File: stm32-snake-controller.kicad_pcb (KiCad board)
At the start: 4 copper layers, 98 x 72 mm, 72 parts, among them J101 Barrel_Jack_MountingPin, J102 JST 2.54 Header, J103 Tag Connector, J301 Conn_01x03, J302 Conn_01x03, J401 Conn_01x07, J402 Conn_01x07, J501 USB_A, Q101 AO3501A, SW101 SW_Push, U101 USBLC6-2SC6, U102 M24C64-RMN, U103 STM32F401RCTx, U201 XC6220B331MR-G, U301 74AHCT1G125, U302 74AHCT1G125, U501 STMPS2141STR, Y101 32.768kHz, Y102 16MHz

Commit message: update BOM
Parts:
- U103: value STM32F401RCTx -> STM32F446RCTx
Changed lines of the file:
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@@
     (fp_line (start 1 0.6) (end -1 0.6)
       (stroke (width 0.1) (type solid)) (layer "F.Fab"))
-    (pad "1" smd roundrect (at -1.025 0 180) (size 1.15 1.4) (layers "F.Cu" "F.Paste" "F.Mask") (roundrect_rratio 0.217391)
+    (pad "1" smd roundrect (at -1.025 0 180) (size 1.15 1.4) (layers "F.Cu" "F.Paste" "F.Mask") (roundrect_rratio 0.2173913043)
       (net 9 "+3.3VA") (pintype "passive"))
-    (pad "2" smd roundrect (at 1.025 0 180) (size 1.15 1.4) (layers "F.Cu" "F.Paste" "F.Mask") (roundrect_rratio 0.217391)
+    (pad "2" smd roundrect (at 1.025 0 180) (size 1.15 1.4) (layers "F.Cu" "F.Paste" "F.Mask") (roundrect_rratio 0.2173913043)
       (net 8 "+3V3") (pintype "passive"))
     (model "${KICAD6_3DMODEL_DIR}/Inductor_SMD.3dshapes/L_0805_2012Metric.wrl"
@@
     (fp_line (start 7.95 2.8) (end 7.95 -1.7)
       (stroke (width 0.1) (type solid)) (layer "F.Fab"))
-    (pad "1" thru_hole roundrect (at 0 0 180) (size 1.2 1.75) (drill 0.75) (layers "*.Cu" "*.Mask") (roundrect_rratio 0.208333)
+    (pad "1" thru_hole roundrect (at 0 0 180) (size 1.2 1.75) (drill 0.75) (layers "*.Cu" "*.Mask") (roundrect_rratio 0.2083333333)
       (net 13 "+5V") (pinfunction "Pin_1") (pintype "passive"))
     (pad "2" thru_hole oval (at 2 0 180) (size 1.2 1.75) (drill 0.75) (layers "*.Cu" "*.Mask")
@@
     (descr "Mounting Hole 3.2mm, no annular, M3")
     (tags "mounting hole 3.2mm no annular m3")
+    (property "LCSC" "")
+    (property "Mouser" "")
     (property "Sheetfile" "stm32-snake-controller.kicad_sch")
     (property "Sheetname" "")
+    (property "exclude_from_bom" "")
     (property "ki_description" "Mounting Hole without connection")
     (property "ki_keywords" "mounting hole")
-    (attr exclude_from_pos_files)
+    (attr exclude_from_pos_files exclude_from_bom)
     (fp_text reference "H102" (at 0 -4.2) (layer "F.SilkS") hide
         (effects (font (size 1 1) (thickness 0.15)))
@@
     (property "Sheetfile" "stm32-snake-controller.kicad_sch")
     (property "Sheetname" "")
+    (property "exclude_from_bom" "")
     (property "ki_description" "DC Barrel Jack with a mounting pin")
     (property "ki_keywords" "DC power barrel jack connector")
-    (attr through_hole)
+    (attr through_hole exclude_from_bom)
     (fp_text reference "J101" (at 0 2.794 180 unlocked) (layer "F.SilkS") hide
         (effects (font (size 1 1) (thickness 0.15)))
@@
     (descr "Mounting Hole 3.2mm, no annular, M3")
     (tags "mounting hole 3.2mm no annular m3")
+    (property "LCSC" "")
+    (property "Mouser" "")
     (property "Sheetfile" "stm32-snake-controller.kicad_sch")
     (property "Sheetname" "")
+    (property "exclude_from_bom" "")
     (property "ki_description" "Mounting Hole without connection")
     (property "ki_keywords" "mounting hole")
-    (attr exclude_from_pos_files)
+    (attr exclude_from_pos_files exclude_from_bom)
     (fp_text reference "H101" (at 0 -4.2) (layer "F.SilkS") hide
         (effects (font (size 1 1) (thickness 0.15)))
@@
   (footprint "User_Footprint:SNES_Controller_Port_Horizontal" (layer "F.Cu")
     (at 175.5 121.805)
+    (property "LCSC" "")
+    (property "Mouser" "")
     (property "Sheetfile" "snes_controller.kicad_sch")
     (property "Sheetname" "snes_controller")
+    (property "exclude_from_bom" "")
     (property "ki_description" "Generic connector, single row, 01x07, script generated (kicad-library-utils/schlib/autogen/connector/)")
     (property "ki_keywords" "connector")
-    (attr through_hole)
+    (attr through_hole exclude_from_bom)
     (fp_text reference "J401" (at -0.018 -3.6 unlocked) (layer "F.SilkS") hide
         (effects (font (size 1 1) (thickness 0.12)))
@@
     (fp_line (start 7.95 2.8) (end 7.95 -1.7)
       (stroke (width 0.1) (type solid)) (layer "F.Fab"))
-    (pad "1" thru_hole roundrect (at 0 0 90) (size 1.2 1.75) (drill 0.75) (layers "*.Cu" "*.Mask") (roundrect_rratio 0.208333)
+    (pad "1" thru_hole roundrect (at 0 0 90) (size 1.2 1.75) (drill 0.75) (layers "*.Cu" "*.Mask") (roundrect_rratio 0.2083333333)
       (net 2 "GND") (pinfunction "GND") (pintype "power_in"))
     (pad "2" thru_hole oval (at 2 0 90) (size 1.2 1.75) (drill 0.75) (layers "*.Cu" "*.Mask")
@@
     (descr "LQFP, 64 Pin (https://www.analog.com/media/en/technical-documentation/data-sheets/ad7606_7606-6_7606-4.pdf), generated with kicad-footprint-generator ipc_gullwing_generator.py")
     (tags "LQFP QFP")
-    (property "LCSC" "C74524")
+    (property "LCSC" "C915971")
     (property "Sheetfile" "stm32-snake-controller.kicad_sch")
     (property "Sheetname" "")
@@
         (effects (font (size 1 1) (thickness 0.15)))
     )
-    (fp_text value "STM32F401RCTx" (at 0 7.4 90) (layer "F.Fab")
+    (fp_text value "STM32F446RCTx" (at 0 7.4 90) (layer "F.Fab")
         (effects (font (size 1 1) (thickness 0.15)))
     )
@@
     (fp_line (start 13.95 2.8) (end 13.95 -1.7)
       (stroke (width 0.1) (type solid)) (layer "F.Fab"))
-    (pad "1" thru_hole roundrect (at 0 0 270) (size 1.2 1.75) (drill 0.75) (layers "*.Cu" "*.Mask") (roundrect_rratio 0.208333)
+    (pad "1" thru_hole roundrect (at 0 0 270) (size 1.2 1.75) (drill 0.75) (layers "*.Cu" "*.Mask") (roundrect_rratio 0.2083333333)
       (net 2 "GND") (pinfunction "GND") (pintype "power_in"))
     (pad "2" thru_hole oval (at 2 0 270) (size 1.2 1.75) (drill 0.75) (layers "*.Cu" "*.Mask")
@@
   (footprint "User_Footprint:SNES_Controller_Port_Horizontal" (layer "F.Cu")
     (at 175.3 77.839 180)
+    (property "LCSC" "")
+    (property "Mouser" "")
     (property "Sheetfile" "snes_controller.kicad_sch")
     (property "Sheetname" "snes_controller")
+    (property "exclude_from_bom" "")
     (property "ki_description" "Generic connector, single row, 01x07, script generated (kicad-library-utils/schlib/autogen/connector/)")
     (property "ki_keywords" "connector")
-    (attr through_hole)
+    (attr through_hole exclude_from_bom)
     (fp_text reference "J402" (at -0.02 -3.4 180 unlocked) (layer "F.SilkS") hide
         (effects (font (size 1 1) (thickness 0.12)))
@@
     (property "Sheetfile" "USB-A_connector.kicad_sch")
     (property "Sheetname" "USB-A_Connector")
+    (property "exclude_from_bom" "")
     (property "ki_description" "USB Type A connector")
     (property "ki_keywords" "connector USB")
-    (attr through_hole)
+    (attr through_hole exclude_from_bom)
     (fp_text reference "J501" (at -1.95 -2.35 90) (layer "F.SilkS") hide
         (effects (font (size 1 1) (thickness 0.15)))
@@
     (descr "Mounting Hole 3.2mm, no annular, M3")
     (tags "mounting hole 3.2mm no annular m3")
+    (property "LCSC" "")
+    (property "Mouser" "")
     (property "Sheetfile" "stm32-snake-controller.kicad_sch")
     (property "Sheetname" "")
+    (property "exclude_from_bom" "")
     (property "ki_description" "Mounting Hole without connection")
     (property "ki_keywords" "mounting hole")
-    (attr exclude_from_pos_files)
+    (attr exclude_from_pos_files exclude_from_bom)
     (fp_text reference "H103" (at 0 -4.2) (layer "F.SilkS") hide
         (effects (font (size 1 1) (thickness 0.15)))
@@
     (descr "Mounting Hole 3.2mm, no annular, M3")
     (tags "mounting hole 3.2mm no annular m3")
+    (property "LCSC" "")
+    (property "Mouser" "")
     (property "Sheetfile" "stm32-snake-controller.kicad_sch")
     (property "Sheetname" "")
+    (property "exclude_from_bom" "")
     (property "ki_description" "Mounting Hole without connection")
     (property "ki_keywords" "mounting hole")
-    (attr exclude_from_pos_files)
+    (attr exclude_from_pos_files exclude_from_bom)
     (fp_text reference "H104" (at 0 -4.2) (layer "F.SilkS") hide
         (effects (font (size 1 1) (thickness 0.15)))

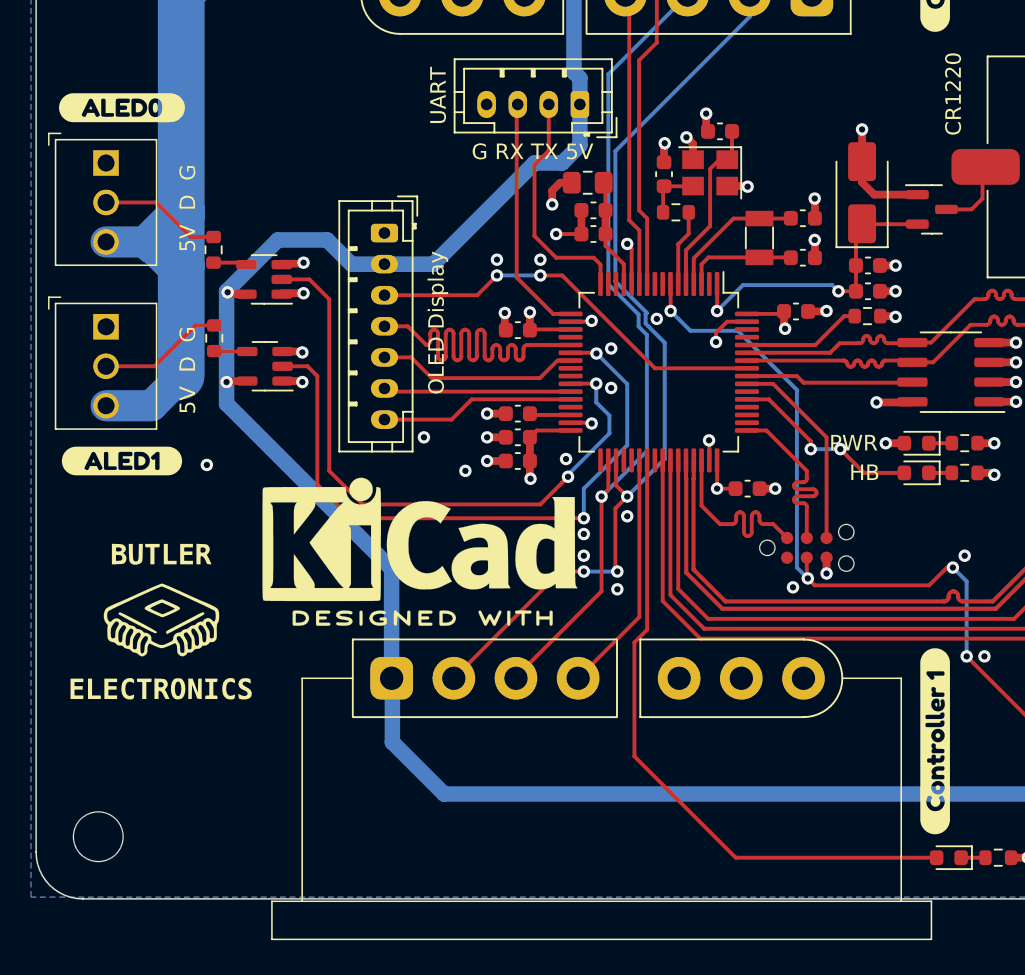
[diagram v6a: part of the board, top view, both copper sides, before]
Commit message: adjust footprint placement
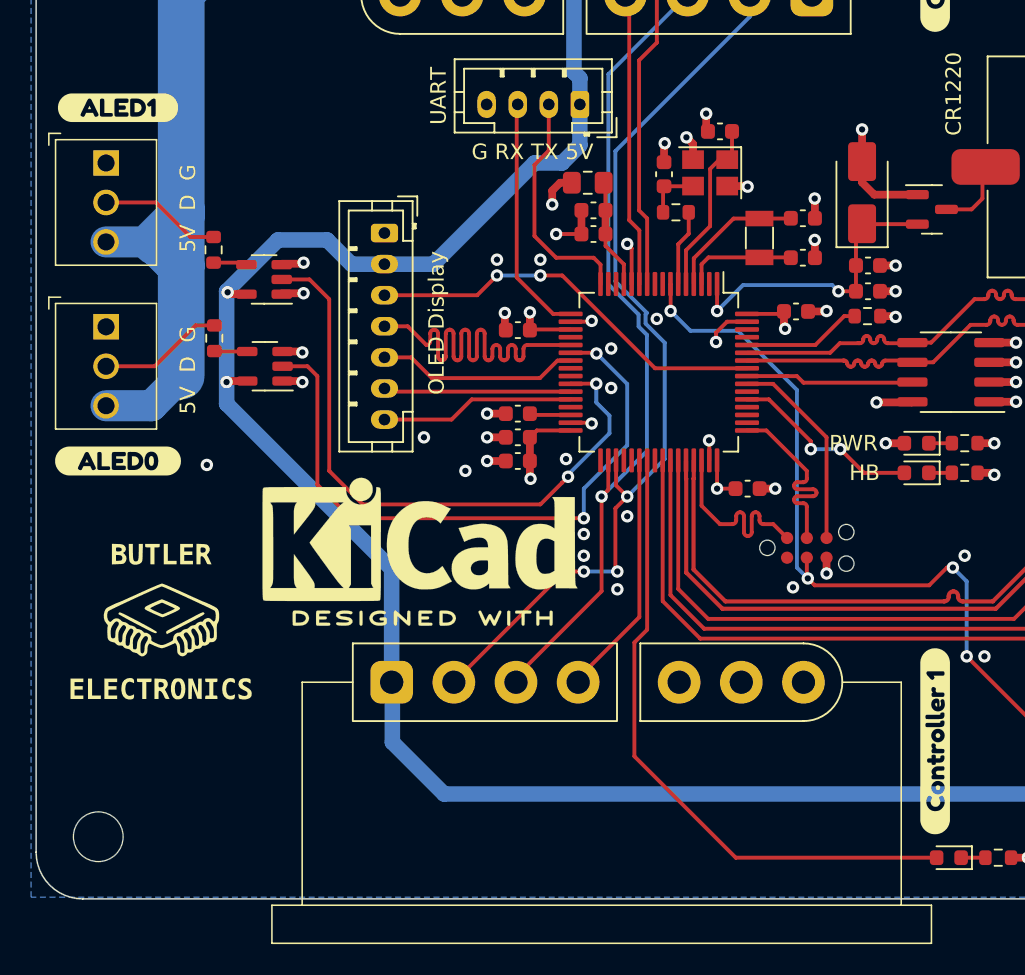
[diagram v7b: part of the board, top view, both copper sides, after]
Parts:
- moved kibuzzard-65A37F11 22.7 mm to (144.3, 107.8)
- moved kibuzzard-65A37F1A 22.7 mm to (144.3, 85.1)
- moved J401 0.25 mm to (175.5, 122.1)
